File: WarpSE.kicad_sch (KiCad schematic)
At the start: 9 parts

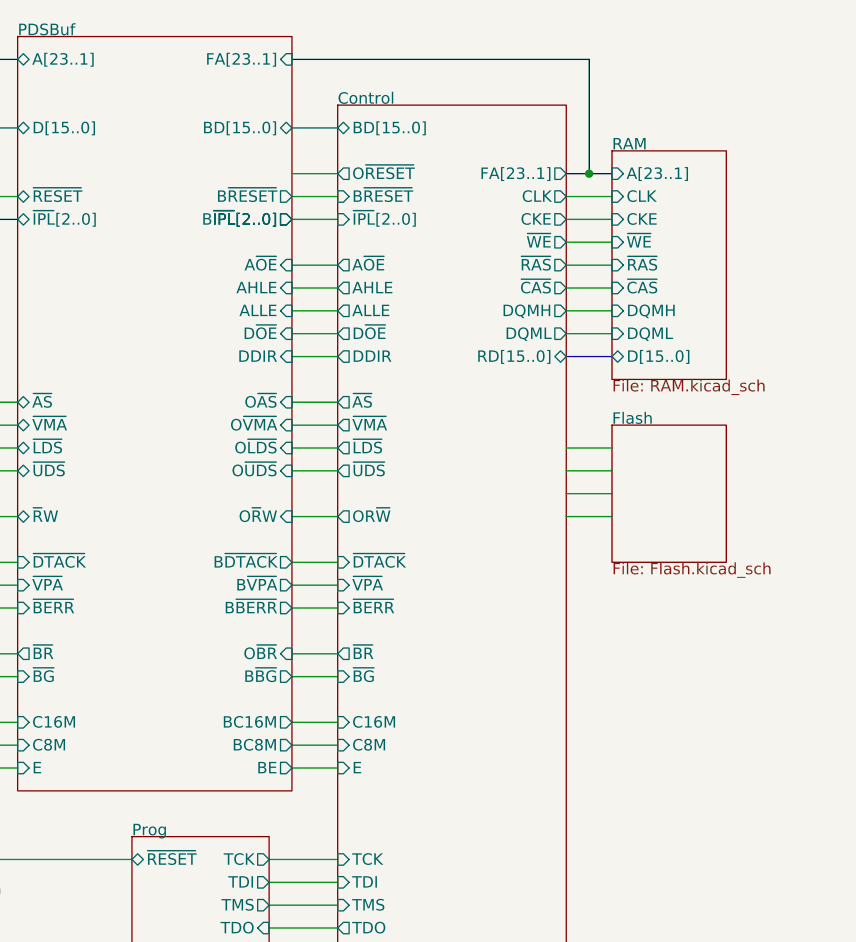
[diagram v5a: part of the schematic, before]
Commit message: better PDS muxing
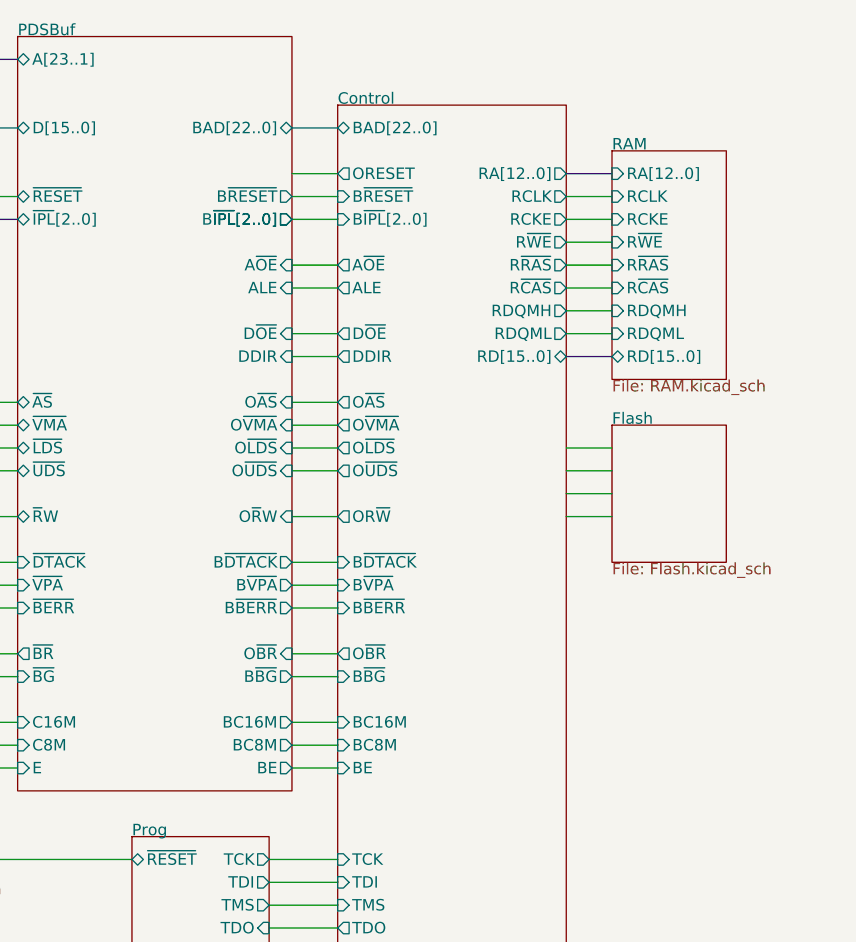
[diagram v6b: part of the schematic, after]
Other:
- sheet Control ports: added ALE, BAD[22..0], BC16M, BC8M, BE, B~{BERR}, B~{BG}, B~{DTACK}, B~{IPL}[2..0], B~{VPA}, ORESET, O~{AS}, O~{BR}, O~{LDS}, O~{UDS}, O~{VMA}, RA[12..0], RCKE, RCLK, RDQMH, RDQML, R~{CAS}, R~{RAS}, R~{WE}; removed AHLE, ALLE, BD[15..0], C16M, C8M, CKE, CLK, DQMH, DQML, E, FA[23..1], O~{RESET}, ~{AS}, ~{BERR}, ~{BG}, ~{BR}, ~{CAS}, ~{DTACK}, ~{IPL}[2..0], ~{LDS}, ~{RAS}, ~{UDS}, ~{VMA}, ~{VPA}, ~{WE}
- sheet PDSBuf ports: added ALE, BAD[22..0]; removed AHLE, ALLE, BD[15..0], FA[23..1]
- sheet RAM ports: added RA[12..0], RCKE, RCLK, RDQMH, RDQML, RD[15..0], R~{CAS}, R~{RAS}, R~{WE}; removed A[23..1], CKE, CLK, DQMH, DQML, D[15..0], ~{CAS}, ~{RAS}, ~{WE}

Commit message: idk
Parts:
- added U1, U15, U16, U26, U27, U4: 74LVC245APW, symbol GW_Logic:74245
- added U10: ATF16V8C-7PU, symbol GW_PLD:GAL16V8
- added U11, U20: 74LVC138APW, symbol GW_Logic:74138
- added U13, U21, U22, U30, U5: 74LVC1G125GW, stdpads:SOT-353, symbol GW_Logic:741G125GW
- added U14, U24, U25, U9: 74LVC04APW, stdpads:TSSOP-14_4.4x5mm_P0.65mm, symbol GW_Logic:7404
- added U17: 74LVC1G86GW, stdpads:SOT-353, symbol GW_Logic:741G86GW
- added U18, U19: 74LVC1G32GW, stdpads:SOT-353, symbol GW_Logic:741G32GW
- added U23: MC68030RC, stdpads:Motorola_CQFP-132, symbol GW_CPU:MC68030RC
- added U28, U8: IS61LV51216, stdpads:TSOP-II-44_400mil_P0.8mm, symbol GW_RAM:SRAM-512Kx16-TSOP2-44
- added U29: ATF22V10C-7PX, symbol GW_PLD:GAL22V10-DIP
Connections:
- new net +3V3: U1.20 (Vcc), U11.16 (Vcc), U11.6 (E3), U13.5 (Vcc), U14.14 (Vcc), U15.1 (AtoB), U15.20 (Vcc), U16.1 (AtoB), U16.20 (Vcc), U17.5 (Vcc), U18.5 (Vcc), U19.5 (Vcc), U20.16 (Vcc), U20.6 (E3), U21.5 (Vcc), U22.5 (Vcc), U24.14 (Vcc), U25.14 (Vcc), U26.20 (Vcc), U27.20 (Vcc), U28.11 (VDD), U28.33 (VDD), U30.5 (Vcc), U4.20 (Vcc), U5.5 (Vcc), U8.11 (VDD), U8.33 (VDD), U9.14 (Vcc)
- new net +5V: U10.20 (Vcc), U29.24 (Vcc)
- new net BA10: U16.18 (B0), U28.27 (A8), U8.27 (A8)
- new net BA11: U16.17 (B1), U28.26 (A9), U8.26 (A9)
- new net BA12: U16.16 (B2), U28.25 (A10), U8.25 (A10)
- new net BA13: U16.15 (B3), U28.24 (A11), U8.24 (A11)
- new net BA14: U16.14 (B4), U28.22 (A12), U8.22 (A12)
- new net BA15: U16.13 (B5), U28.21 (A13), U8.21 (A13)
- new net BA16: U16.12 (B6), U28.20 (A14), U8.20 (A14)
- new net BA17: U16.11 (B7), U28.19 (A15), U8.19 (A15)
- new net BA2: U15.18 (B0), U28.5 (A0), U8.5 (A0)
- new net BA3: U15.17 (B1), U28.4 (A1), U8.4 (A1)
- new net BA4: U15.16 (B2), U28.3 (A2), U8.3 (A2)
- new net BA5: U15.15 (B3), U28.2 (A3), U8.2 (A3)
- new net BA6: U15.14 (B4), U28.1 (A4), U8.1 (A4)
- new net BA7: U15.13 (B5), U28.44 (A5), U8.44 (A5)
- new net BA8: U15.12 (B6), U28.43 (A6), U8.43 (A6)
- new net BA9: U15.11 (B7), U28.42 (A7), U8.42 (A7)
- new net BAS: U25.6 (3Y)
- new net BA~{OE}: U15.19 (~{OE}), U16.19 (~{OE})
- new net BD0: U1.2 (A0), U8.7 (D0)
- new net BD1: U1.3 (A1), U8.8 (D1)
- new net BD10: U4.4 (A2), U8.31 (D10)
- new net BD11: U4.5 (A3), U8.32 (D11)
- new net BD12: U4.6 (A4), U8.35 (D12)
- new net BD13: U4.7 (A5), U8.36 (D13)
- new net BD14: U4.8 (A6), U8.37 (D14)
- new net BD15: U4.9 (A7), U8.38 (D15)
- new net BD16: U26.2 (A0), U28.7 (D0)
- new net BD17: U26.3 (A1), U28.8 (D1)
- new net BD18: U26.4 (A2), U28.9 (D2)
- new net BD19: U26.5 (A3), U28.10 (D3)
- new net BD2: U1.4 (A2), U8.9 (D2)
- new net BD20: U26.6 (A4), U28.13 (D4)
- new net BD21: U26.7 (A5), U28.14 (D5)
- new net BD22: U26.8 (A6), U28.15 (D6)
- new net BD23: U26.9 (A7), U28.16 (D7)
- new net BD24: U27.2 (A0), U28.29 (D8)
- new net BD25: U27.3 (A1), U28.30 (D9)
- new net BD26: U27.4 (A2), U28.31 (D10)
- new net BD27: U27.5 (A3), U28.32 (D11)
- new net BD28: U27.6 (A4), U28.35 (D12)
- new net BD29: U27.7 (A5), U28.36 (D13)
- new net BD3: U1.5 (A3), U8.10 (D3)
- new net BD30: U27.8 (A6), U28.37 (D14)
- new net BD31: U27.9 (A7), U28.38 (D15)
- new net BD4: U1.6 (A4), U8.13 (D4)
- new net BD5: U1.7 (A5), U8.14 (D5)
- new net BD6: U1.8 (A6), U8.15 (D6)
- new net BD7: U1.9 (A7), U8.16 (D7)
- new net BD8: U4.2 (A0), U8.29 (D8)
- new net BD9: U4.3 (A1), U8.30 (D9)
- new net BD~{OE}: U1.19 (~{OE}), U26.19 (~{OE}), U27.19 (~{OE}), U29.20 (I/O), U4.19 (~{OE}), U5.4 (Y)
- new net BRMC: U25.4 (2Y)
- new net B~{A}0: U24.8 (4Y)
- new net B~{A}1: U24.6 (3Y)
- new net B~{A}18: U24.4 (2Y)
- new net B~{A}19: U24.2 (1Y)
- new net B~{A}20: U14.12 (6Y)
- new net B~{A}21: U14.10 (5Y)
- new net B~{A}22: U14.8 (4Y)
- new net B~{A}23: U14.6 (3Y)
- new net B~{A}24: U14.4 (2Y)
- new net B~{A}25: U14.2 (1Y)
- new net B~{A}26: U9.12 (6Y)
- new net B~{A}27: U9.10 (5Y)
- new net B~{A}28: U9.8 (4Y)
- new net B~{A}29: U9.6 (3Y)
- new net B~{A}30: U9.4 (2Y)
- new net B~{A}31: U9.2 (1Y)
- new net B~{CBREQ}: U19.4 (Y)
- new net B~{FC}0: U25.12 (6Y)
- new net B~{FC}1: U25.10 (5Y)
- new net B~{FC}2: U25.8 (4Y)
- new net B~{R}W: U25.2 (1Y)
- new net B~{SIZ}0: U24.10 (5Y)
- new net B~{SIZ}1: U24.12 (6Y)
- new net DBD~{OE}: U29.1 (CLK/IN), U5.2 (A)
- new net DC~{OE}: U13.1 (~{OE}), U29.21 (I/O), U30.1 (~{OE}), U5.1 (~{OE})
- new net D~{CBACK}: U29.3 (IN), U30.2 (A)
- new net D~{STERM}: U13.2 (A), U29.2 (IN)
- new net FA0: U24.9 (4A)
- new net FA1: U24.5 (3A)
- new net FA10: U16.2 (A0)
- new net FA11: U16.3 (A1)
- new net FA12: U16.4 (A2)
- new net FA13: U10.17 (I/O), U16.5 (A3)
- new net FA14: U10.14 (I/O), U16.6 (A4)
- new net FA15: U10.13 (I/O), U16.7 (A5)
- new net FA16: U10.9 (IN), U16.8 (A6)
- new net FA17: U10.8 (IN), U16.9 (A7)
- new net FA18: U10.7 (IN), U18.1 (A), U24.3 (2A), U29.9 (IN)
- new net FA19: U10.6 (IN), U20.4 (~{E1}), U24.1 (1A)
- new net FA2: U15.2 (A0)
- new net FA20: U14.13 (6A), U20.5 (~{E2})
- new net FA21: U14.11 (5A), U20.3 (A2)
- new net FA22: U14.9 (4A), U20.2 (A1)
- new net FA23: U14.5 (3A), U20.1 (A0)
- new net FA24: U11.5 (~{E2}), U14.3 (2A)
- new net FA25: U11.3 (A2), U14.1 (1A)
- new net FA26: U11.2 (A1), U9.13 (6A)
- new net FA27: U11.1 (A0), U9.11 (5A)
- new net FA28: U29.16 (I/O), U9.9 (4A)
- new net FA29: U18.2 (B), U29.8 (IN), U9.5 (3A)
- new net FA3: U15.3 (A1)
- new net FA30: U17.2 (B), U29.7 (IN), U9.3 (2A)
- new net FA31: U17.1 (A), U29.6 (IN), U9.1 (1A)
- new net FA4: U15.4 (A2)
- new net FA5: U15.5 (A3)
- new net FA6: U15.6 (A4)
- new net FA7: U15.7 (A5)
- new net FA8: U15.8 (A6)
- new net FA9: U15.9 (A7)
- new net FCPUCLK: U10.1 (CLK/IN)
- new net FD0: U1.18 (B0)
- new net FD1: U1.17 (B1)
- new net FD10: U4.16 (B2)
- new net FD11: U4.15 (B3)
- new net FD12: U4.14 (B4)
- new net FD13: U4.13 (B5)
- new net FD14: U4.12 (B6)
- new net FD15: U4.11 (B7)
- new net FD16: U26.18 (B0)
- new net FD17: U26.17 (B1)
- new net FD18: U26.16 (B2)
- new net FD19: U26.15 (B3)
- new net FD2: U1.16 (B2)
- new net FD20: U26.14 (B4)
- new net FD21: U26.13 (B5)
- new net FD22: U26.12 (B6)
- new net FD23: U26.11 (B7)
- new net FD24: U27.18 (B0)
- new net FD25: U27.17 (B1)
- new net FD26: U27.16 (B2)
- new net FD27: U27.15 (B3)
- new net FD28: U27.14 (B4)
- new net FD29: U27.13 (B5)
- new net FD3: U1.15 (B3)
- new net FD30: U27.12 (B6)
- new net FD31: U27.11 (B7)
- new net FD4: U1.14 (B4)
- new net FD5: U1.13 (B5)
- new net FD6: U1.12 (B6)
- new net FD7: U1.11 (B7)
- new net FD8: U4.18 (B0)
- new net FD9: U4.17 (B1)
- new net FFC0: U10.5 (IN), U25.13 (6A), U29.13 (IN)
- new net FFC1: U10.4 (IN), U25.11 (5A), U29.11 (IN)
- new net FFC2: U10.3 (IN), U25.9 (4A), U29.10 (IN)
- new net FFPU~{CS}: U10.19 (I/O)
- new net FMODE: U10.18 (I/O)
- new net FR~{W}: U1.1 (AtoB), U25.1 (1A), U29.5 (IN)
- new net FSIZ0: U24.11 (5A)
- new net FSIZ1: U24.13 (6A)
- new net F~{AS}: U10.2 (IN), U25.5 (3A), U29.4 (IN)
- new net F~{CBACK}: U29.18 (I/O), U30.4 (Y)
- new net F~{CBREQ}: U19.1 (A)
- new net F~{RMC}: U25.3 (2A)
- new net F~{STERM}: U13.4 (Y), U29.19 (I/O)
- new net GBDOEEN: U29.22 (I/O)
- new net GND: U1.10 (GND), U10.10 (GND), U11.4 (~{E1}), U11.8 (GND), U13.3 (GND), U14.7 (GND), U15.10 (GND), U16.10 (GND), U17.3 (GND), U18.3 (GND), U19.2 (B), U19.3 (GND), U20.8 (GND), U21.3 (GND), U22.3 (GND), U24.7 (GND), U25.7 (GND), U26.10 (GND), U27.10 (GND), U28.12 (GND), U28.28 (A18), U28.34 (GND), U28.6 (~{CE}), U29.12 (GND), U30.3 (GND), U4.10 (GND), U5.3 (GND), U8.12 (GND), U8.28 (A18), U8.34 (GND), U8.6 (~{CE}), U9.7 (GND)
- new net GSTERMEN: U29.17 (I/O)
- new net KA18: U21.4 (Y), U28.18 (A16), U8.18 (A16)
- new net KA19: U22.4 (Y), U28.23 (A17), U8.23 (A17)
- new net KGA18: U18.4 (Y), U21.2 (A)
- new net KGA19: U17.4 (Y), U22.2 (A)
- new net L2A~{OE}: U21.1 (~{OE}), U22.1 (~{OE})
- new net L2M0: U8.40 (~{UB})
- new net L2M1: U8.39 (~{LB})
- new net L2M2: U28.40 (~{UB})
- new net L2M3: U28.39 (~{LB})
- new net L2~{OE}: U28.41 (~{OE}), U8.41 (~{OE})
- new net L2~{WE}: U28.17 (~{WE}), U8.17 (~{WE})
- new net RAM~{CS}: U11.15 (~{Q0}), U29.15 (I/O)
- new net RV~{CS}: U20.15 (~{Q0}), U29.23 (I/O)
- new net VRAM~{CS}: U11.7 (~{Q7}), U29.14 (I/O)
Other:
- note added: "RAMCS = A[31:28]==4'h0 && A[27:24]==4'h0 && A[23:20]==4'h0 && A[19:18]==2'b00 ROMCS = A[31:28]==4'h4 && A[27:24]==4'h0 && A[23:20]==4'h8 && A[19]==1'b0 VRAMCS = A[31:28]==4'hF && A[27:24]==4'hE && A[23:20]==4'h0 && A[19:18]==2'b00 RAMCS || ROMCS || VRAMCS = A[24]==1'b0 && A[22:20]==3'h0 && A[19]==1'b0;"
- moved on the sheet: FID1, FID2, FID3, FID4, H1, H2, H3, H4, H5

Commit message: more
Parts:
- removed U1, U15, U16, U26, U27, U4: 74LVC245APW, symbol GW_Logic:74245
- removed U10: ATF16V8C-7PU, symbol GW_PLD:GAL16V8
- removed U11, U20: 74LVC138APW, symbol GW_Logic:74138
- removed U13, U21, U22, U30, U5: 74LVC1G125GW, stdpads:SOT-353, symbol GW_Logic:741G125GW
- removed U14, U24, U25, U9: 74LVC04APW, stdpads:TSSOP-14_4.4x5mm_P0.65mm, symbol GW_Logic:7404
- removed U17: 74LVC1G86GW, stdpads:SOT-353, symbol GW_Logic:741G86GW
- removed U18, U19: 74LVC1G32GW, stdpads:SOT-353, symbol GW_Logic:741G32GW
- removed U23: MC68030RC, stdpads:Motorola_CQFP-132, symbol GW_CPU:MC68030RC
- removed U28, U8: IS61LV51216, stdpads:TSOP-II-44_400mil_P0.8mm, symbol GW_RAM:SRAM-512Kx16-TSOP2-44
- removed U29: ATF22V10C-7PX, symbol GW_PLD:GAL22V10-DIP
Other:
- sheet Control ports: added FCK, FMISO, FMOSI, F~{CS}, RBA[1..0]; removed none
- sheet RAM ports: added RBA[1..0]; removed none
- note removed: "RAMCS = A[31:28]==4'h0 && A[27:24]==4'h0 && A[23:20]==4'h0 && A[19:18]==2'b00 ROMCS = A[31:28]==4'h4 && A[27:24]==4'h0 && A[23:20]==4'h8 && A[19]==1'b0 VRAMCS = A[31:28]==4'hF && A[27:24]==4'hE && A[23:20]==4'h0 && A[19:18]==2'b00 RAMCS || ROMCS || VRAMCS = A[24]==1'b0 && A[22:20]==3'h0 && A[19]==1'b0;"
